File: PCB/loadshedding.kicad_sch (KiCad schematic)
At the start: 80 parts, among them Q1 BC557, Q2 BC557, Q3 BC557, Q4 BC557, Q5 BC557, Q6 BC557, Q7 BC557

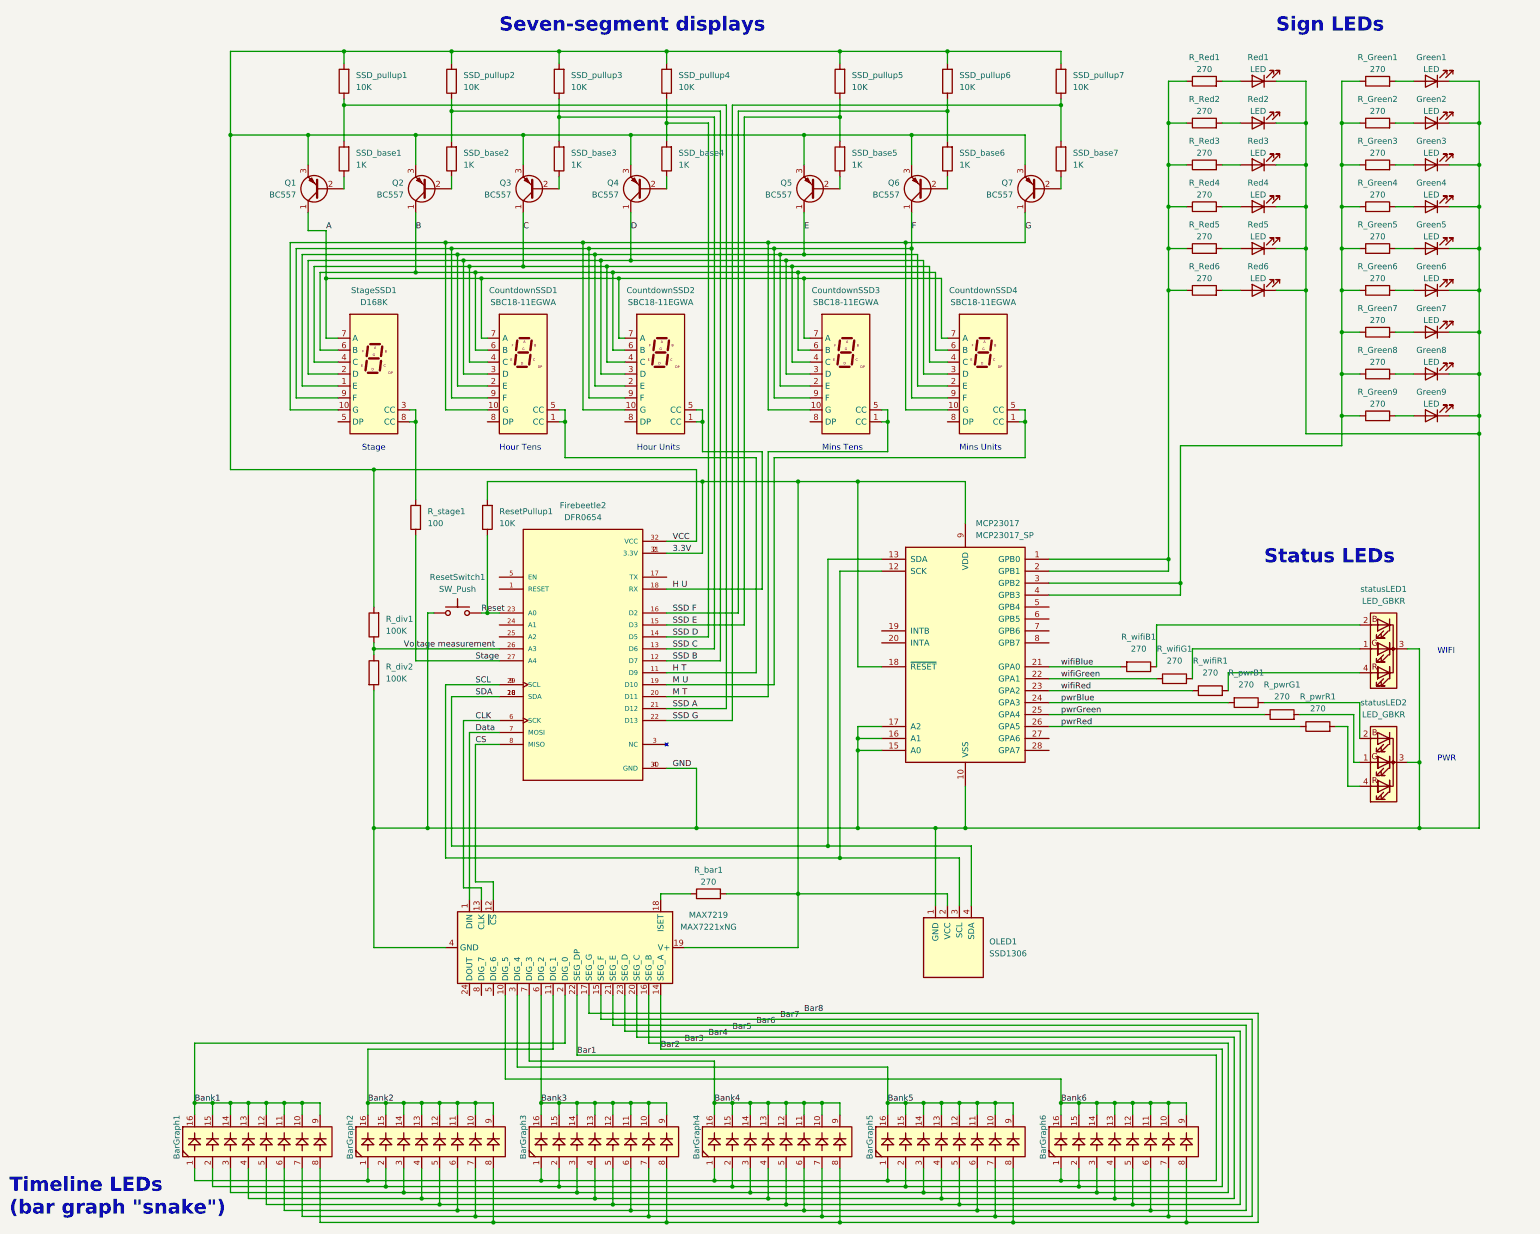
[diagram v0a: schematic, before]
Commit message: Update resistor values
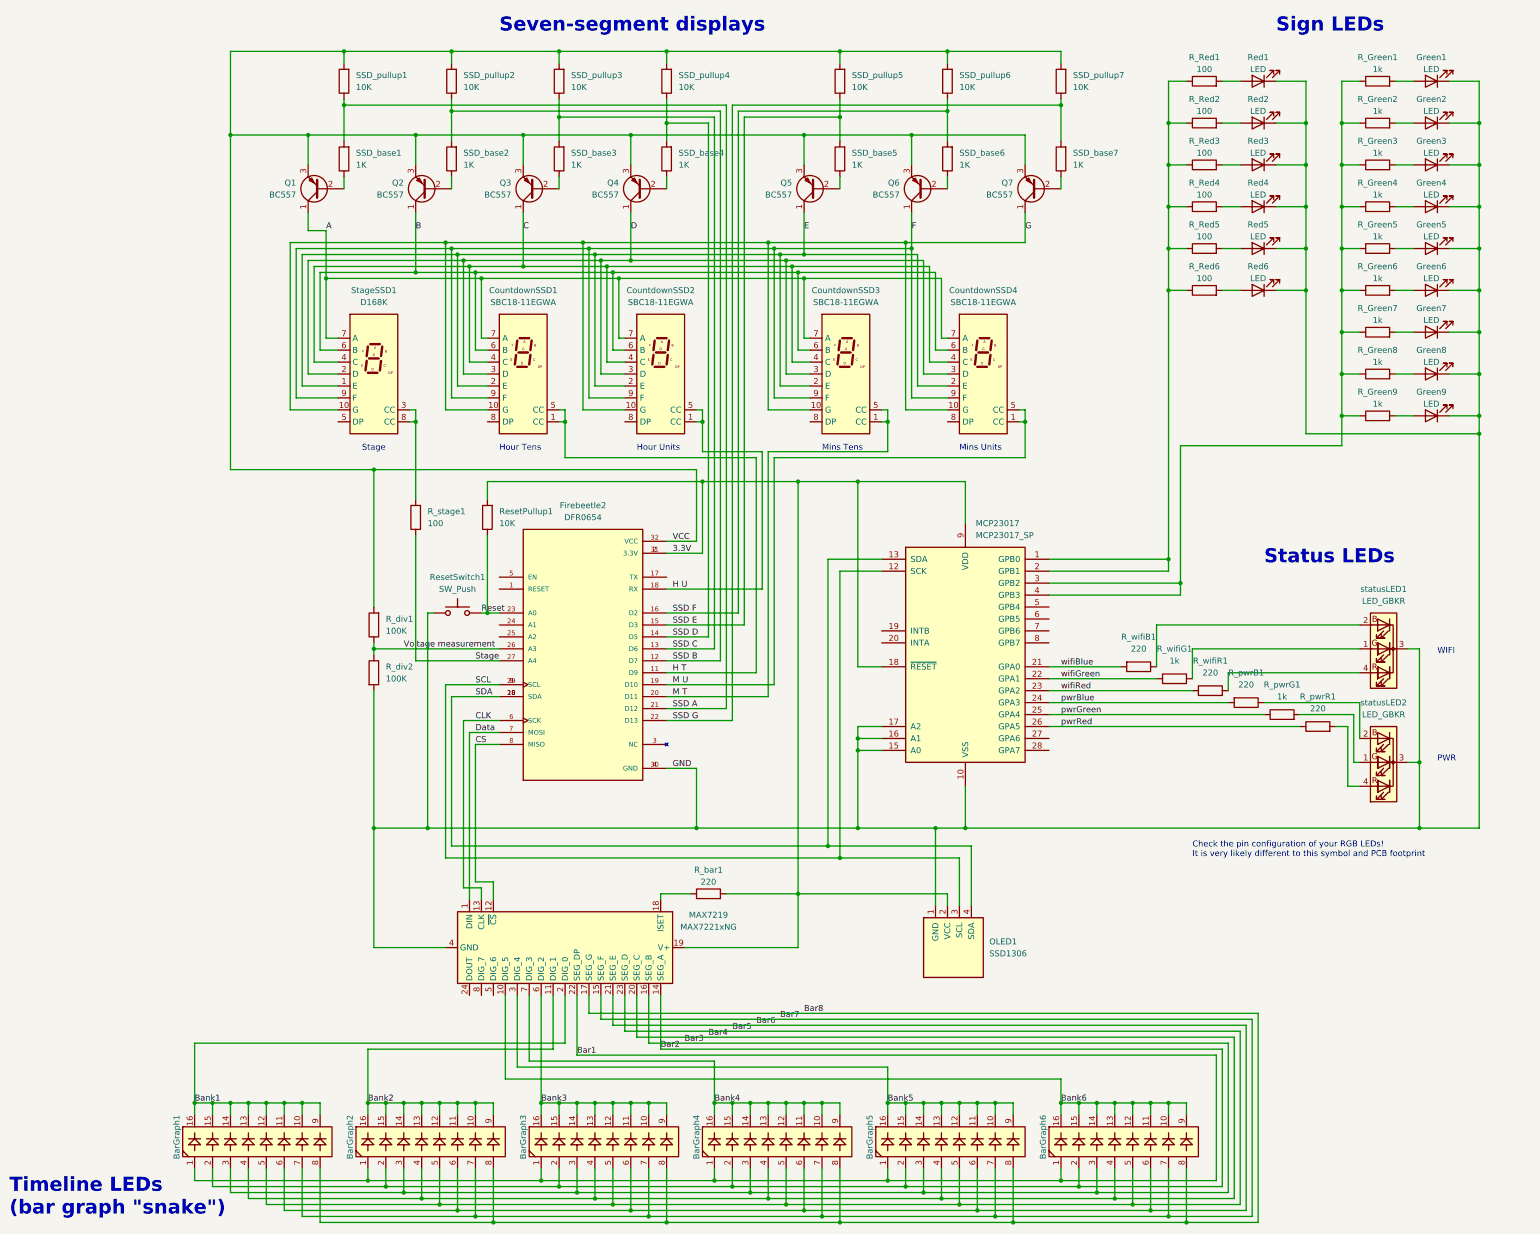
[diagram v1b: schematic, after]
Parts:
- R_Green1, R_Green2, R_Green3, R_Green4, R_Green5, R_Green6, R_Green7, R_Green8, R_Green9, R_pwrG1, R_wifiG1: value 270 -> 1k
- R_Red1, R_Red2, R_Red3, R_Red4, R_Red5, R_Red6: value 270 -> 100
- R_bar1, R_pwrB1, R_pwrR1, R_wifiB1, R_wifiR1: value 270 -> 220
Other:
- note added: "Check the pin configuration of your RGB LEDs! It is very likely different to this symbol and PCB footprint"
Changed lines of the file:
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@@
+    (effects (font (size 1.27 1.27)) (justify left bottom))
+  )
+  (text "Check the pin configuration of your RGB LEDs! \nIt is very likely different to this symbol and PCB footprint"
+    (at 273.05 200.66 0)
     (effects (font (size 1.27 1.27)) (justify left bottom))
   )
@@
       (effects (font (size 1.27 1.27)))
     )
-    (property "Value" "270" (at 284.48 163.83 90)
+    (property "Value" "220" (at 284.48 163.83 90)
       (effects (font (size 1.27 1.27)))
     )
@@
       (effects (font (size 1.27 1.27)))
     )
-    (property "Value" "270" (at 275.59 59.69 90)
+    (property "Value" "100" (at 275.59 59.69 90)
       (effects (font (size 1.27 1.27)))
     )
@@
       (effects (font (size 1.27 1.27)))
     )
-    (property "Value" "270" (at 312.42 41.91 90)
+    (property "Value" "1k" (at 312.42 41.91 90)
       (effects (font (size 1.27 1.27)))
     )
@@
       (effects (font (size 1.27 1.27)))
     )
-    (property "Value" "270" (at 312.42 50.8 90)
+    (property "Value" "1k" (at 312.42 50.8 90)
       (effects (font (size 1.27 1.27)))
     )
@@
       (effects (font (size 1.27 1.27)))
     )
-    (property "Value" "270" (at 312.42 77.47 90)
+    (property "Value" "1k" (at 312.42 77.47 90)
       (effects (font (size 1.27 1.27)))
     )
@@
       (effects (font (size 1.27 1.27)))
     )
-    (property "Value" "270" (at 275.59 41.91 90)
+    (property "Value" "100" (at 275.59 41.91 90)
       (effects (font (size 1.27 1.27)))
     )
@@
       (effects (font (size 1.27 1.27)))
     )
-    (property "Value" "270" (at 312.42 104.14 90)
+    (property "Value" "1k" (at 312.42 104.14 90)
       (effects (font (size 1.27 1.27)))
     )
@@
       (effects (font (size 1.27 1.27)))
     )
-    (property "Value" "270" (at 312.42 95.25 90)
+    (property "Value" "1k" (at 312.42 95.25 90)
       (effects (font (size 1.27 1.27)))
     )
@@
       (effects (font (size 1.27 1.27)))
     )
-    (property "Value" "270" (at 312.42 68.58 90)
+    (property "Value" "1k" (at 312.42 68.58 90)
       (effects (font (size 1.27 1.27)))
     )
@@
       (effects (font (size 1.27 1.27)))
     )
-    (property "Value" "270" (at 269.24 158.75 90)
+    (property "Value" "1k" (at 269.24 158.75 90)
       (effects (font (size 1.27 1.27)))
     )
@@
       (effects (font (size 1.27 1.27)))
     )
-    (property "Value" "270" (at 275.59 50.8 90)
+    (property "Value" "100" (at 275.59 50.8 90)
       (effects (font (size 1.27 1.27)))
     )
@@
       (effects (font (size 1.27 1.27)))
     )
-    (property "Value" "270" (at 312.42 59.69 90)
+    (property "Value" "1k" (at 312.42 59.69 90)
       (effects (font (size 1.27 1.27)))
     )
@@
       (effects (font (size 1.27 1.27)))
     )
-    (property "Value" "270" (at 312.42 33.02 90)
+    (property "Value" "1k" (at 312.42 33.02 90)
       (effects (font (size 1.27 1.27)))
     )
@@
       (effects (font (size 1.27 1.27)))
     )
-    (property "Value" "270" (at 312.42 86.36 90)
+    (property "Value" "1k" (at 312.42 86.36 90)
       (effects (font (size 1.27 1.27)))
     )
@@
       (effects (font (size 1.27 1.27)))
     )
-    (property "Value" "270" (at 292.1 166.37 90)
+    (property "Value" "1k" (at 292.1 166.37 90)
       (effects (font (size 1.27 1.27)))
     )
@@
       (effects (font (size 1.27 1.27)))
     )
-    (property "Value" "270" (at 170.18 205.74 90)
+    (property "Value" "220" (at 170.18 205.74 90)
       (effects (font (size 1.27 1.27)))
     )
@@
       (effects (font (size 1.27 1.27)))
     )
-    (property "Value" "270" (at 275.59 77.47 90)
+    (property "Value" "100" (at 275.59 77.47 90)
       (effects (font (size 1.27 1.27)))
     )
@@
       (effects (font (size 1.27 1.27)))
     )
-    (property "Value" "270" (at 275.59 68.58 90)
+    (property "Value" "100" (at 275.59 68.58 90)
       (effects (font (size 1.27 1.27)))
     )
@@
       (effects (font (size 1.27 1.27)))
     )
-    (property "Value" "270" (at 276.86 161.29 90)
+    (property "Value" "220" (at 276.86 161.29 90)
       (effects (font (size 1.27 1.27)))
     )
@@
       (effects (font (size 1.27 1.27)))
     )
-    (property "Value" "270" (at 261.62 156.21 90)
+    (property "Value" "220" (at 261.62 156.21 90)
       (effects (font (size 1.27 1.27)))
     )
@@
       (effects (font (size 1.27 1.27)))
     )
-    (property "Value" "270" (at 275.59 33.02 90)
+    (property "Value" "100" (at 275.59 33.02 90)
       (effects (font (size 1.27 1.27)))
     )
@@
       (effects (font (size 1.27 1.27)))
     )
-    (property "Value" "270" (at 299.72 168.91 90)
-      (effects (font (size 1.27 1.27)))
-    )
+    (property "Value" "220" (at 299.72 168.91 90)
+      (effects (font (size 1.27 1.27)))
+    )
